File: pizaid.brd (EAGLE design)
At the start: 44 parts, among them X1 S4B-ZR, X2 DCJACK-R

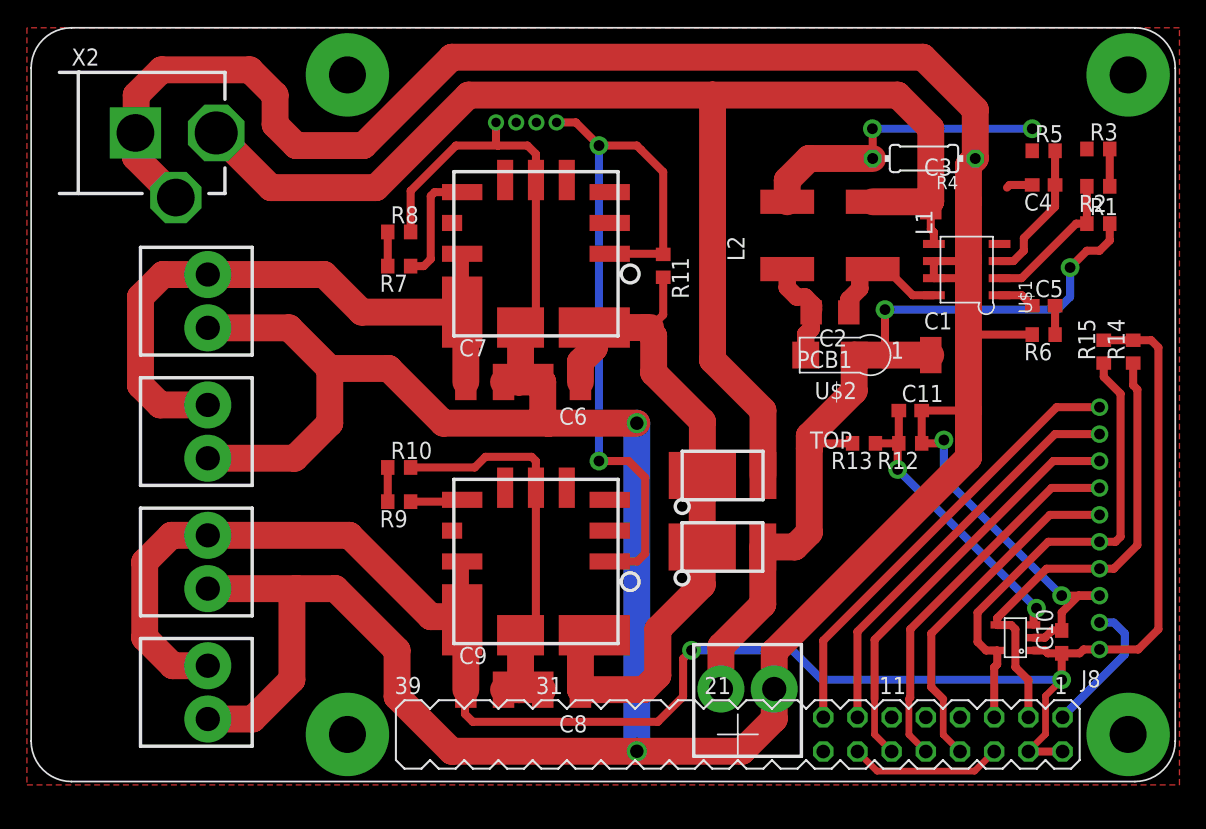
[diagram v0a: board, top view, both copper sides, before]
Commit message: modified to two-layer pcb and generated gerber for fusion
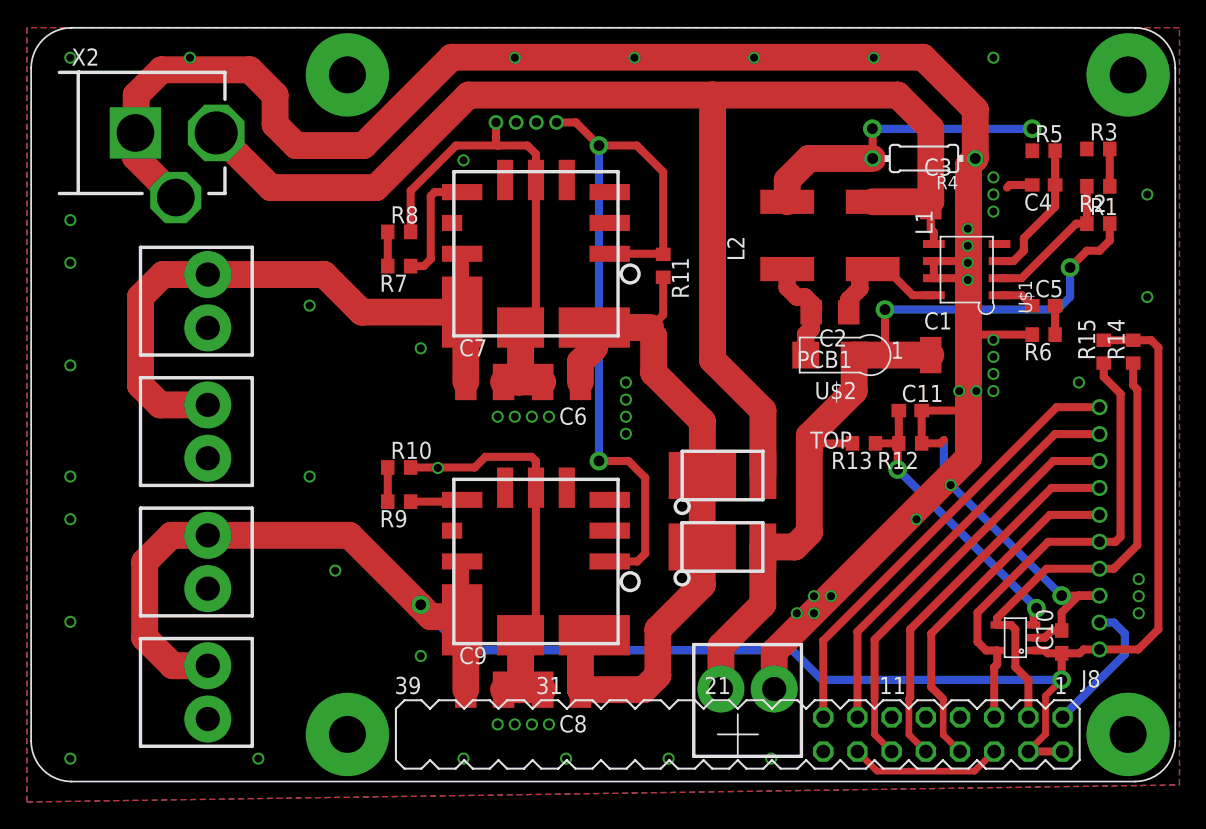
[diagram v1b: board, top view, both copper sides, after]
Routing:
- net GND: track 385.3 -> 242.0 mm, vias 4 -> 64
- net 5V0@2: track 145.3 -> 144.2 mm
- added copper zone on layer 16, net GND

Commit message: cleaned board
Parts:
- R11: value (none) -> 10k
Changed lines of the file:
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@@
 <attribute name="OC_FARNELL" value="9491830" x="40.225" y="52.3425" size="1.778" layer="28" rot="MR180" display="off"/>
 </element>
-<element name="R11" library="rcl" package="R0603" value="" x="50.3975" y="41.69" rot="R270"/>
+<element name="R11" library="rcl" package="R0603" value="10k" x="50.3975" y="41.69" rot="R270"/>
 <element name="U$8" library="pizaid" package="B2P-VH" value="B2P-VH" x="16.5625" y="29.375" rot="R270"/>
 <element name="U$9" library="pizaid" package="B2P-VH" value="B2P-VH" x="16.5625" y="10" rot="R270"/>
